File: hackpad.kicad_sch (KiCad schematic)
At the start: 33 parts, among them SW1 SW_Push, SW10 SW_Push, SW11 SW_Push, SW12 SW_Push, SW13 SW_Push, SW14 SW_Push, SW15 SW_Push, SW16 SW_Push, SW2 SW_Push, SW3 SW_Push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

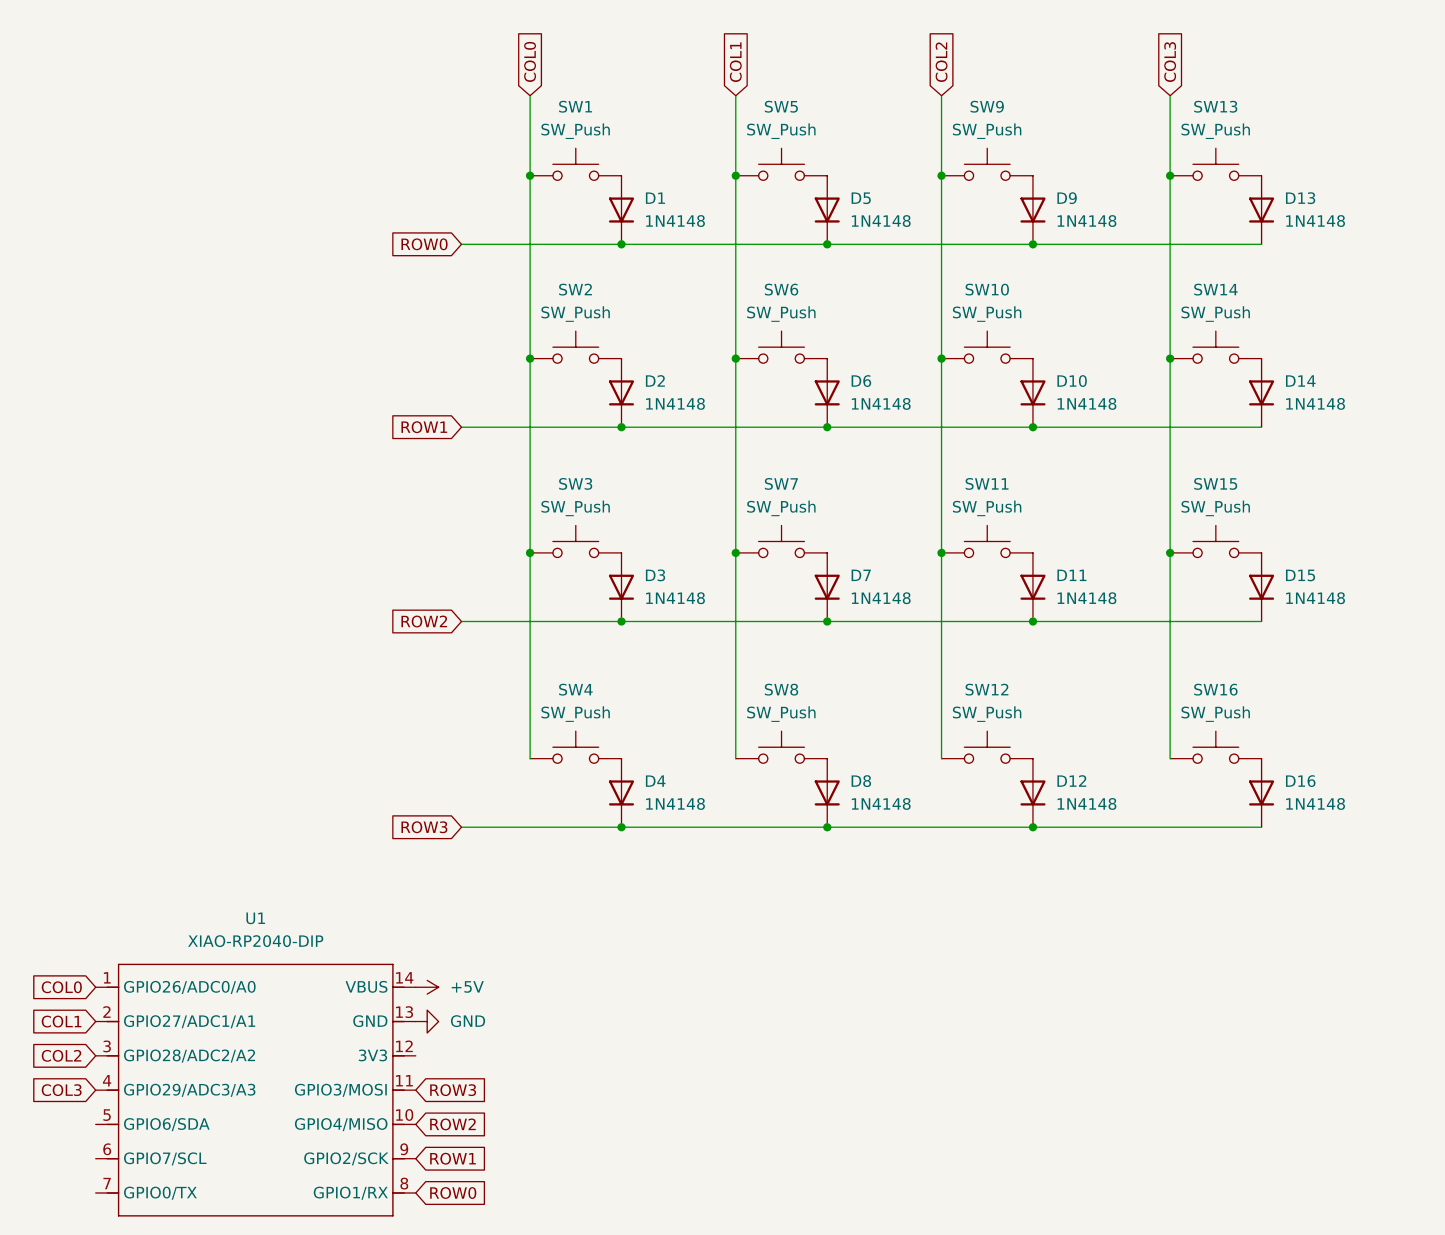
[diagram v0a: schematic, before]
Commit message: Updated switch 8 to 2u size
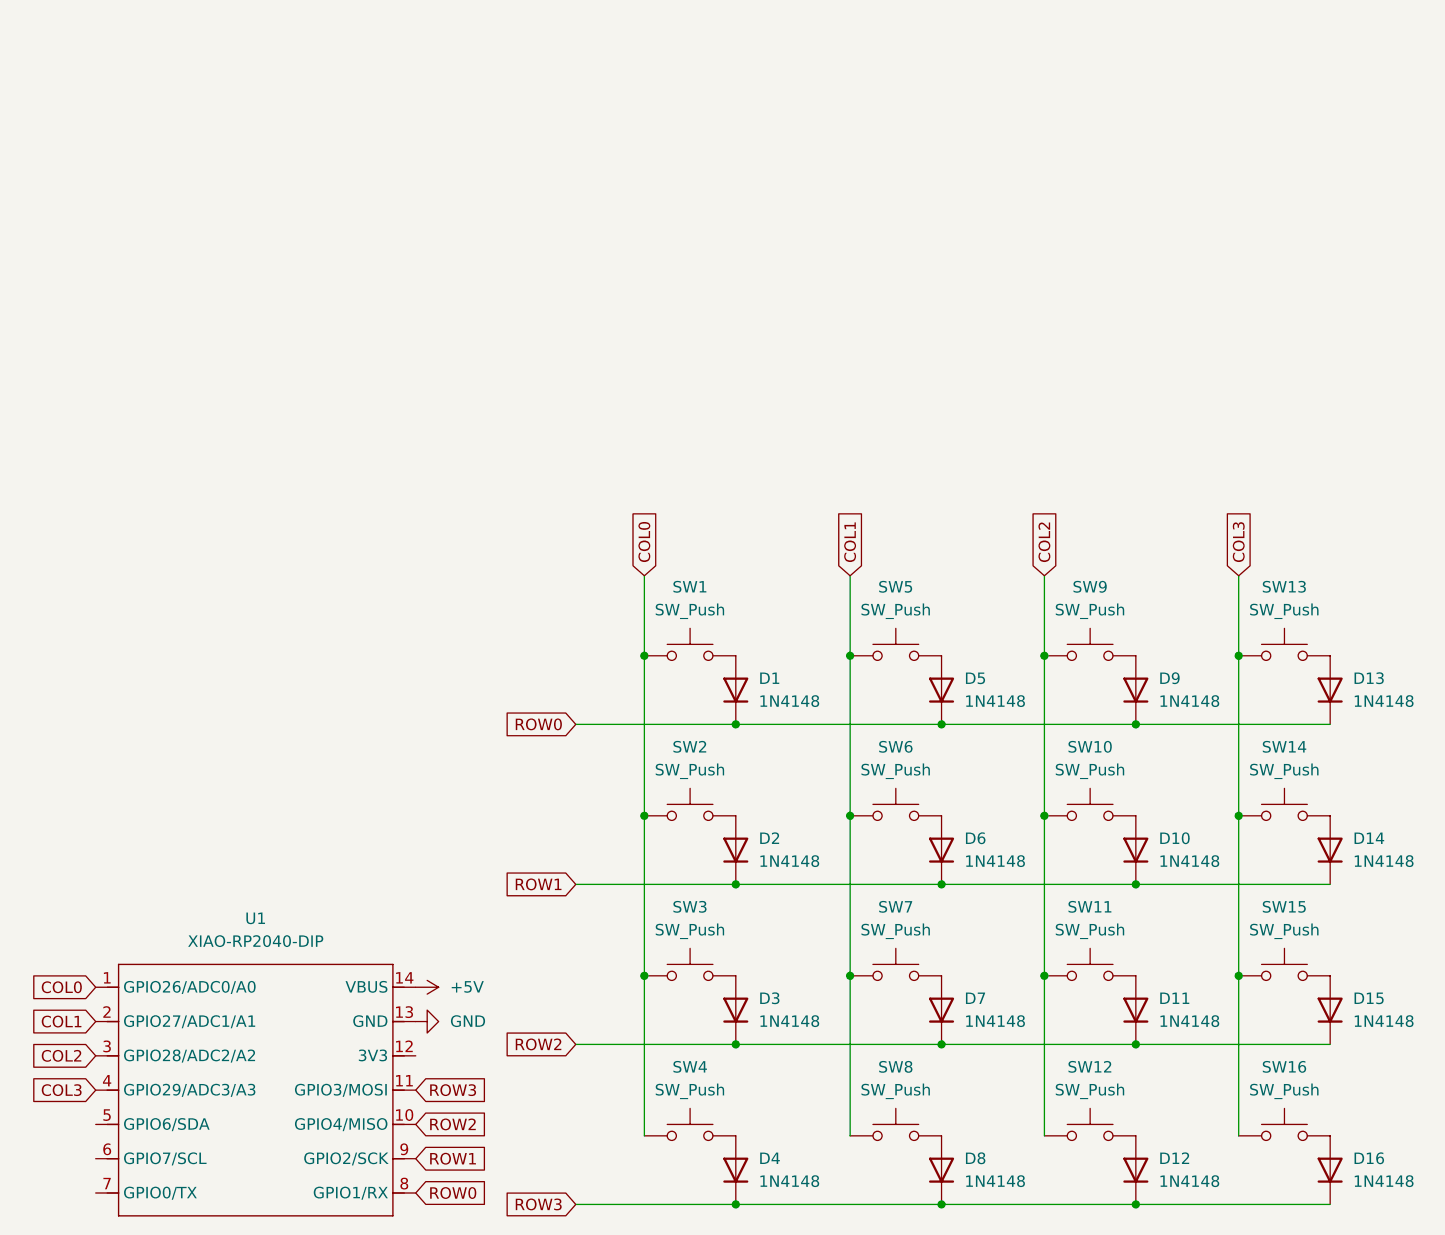
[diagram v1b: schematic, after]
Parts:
- SW8: footprint Button_Switch_Keyboard:SW_Cherry_MX_1.00u_PCB -> Button_Switch_Keyboard:SW_Cherry_MX_2.00u_PCB
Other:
- moved on the sheet: D1, D10, D11, D12, D13, D14, D15, D16, D2, D3, D4, D5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
